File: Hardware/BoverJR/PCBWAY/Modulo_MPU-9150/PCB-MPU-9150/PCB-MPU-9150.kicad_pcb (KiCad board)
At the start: 2 copper layers, 15 x 20 mm, 16 parts, among them P1 CONN_01X08, U1 MPU-9150, U2 AP2112K-3.3

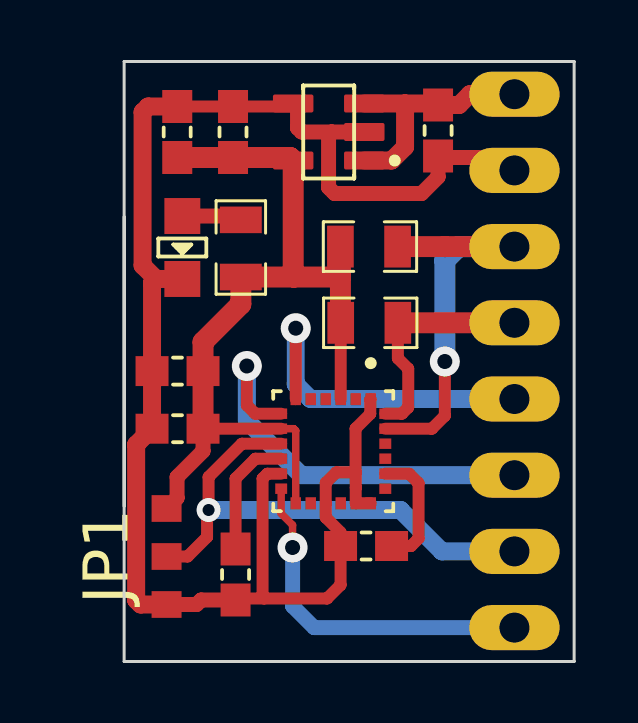
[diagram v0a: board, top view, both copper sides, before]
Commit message: esperando verificacion de pcbway ya cargue 6 gerber
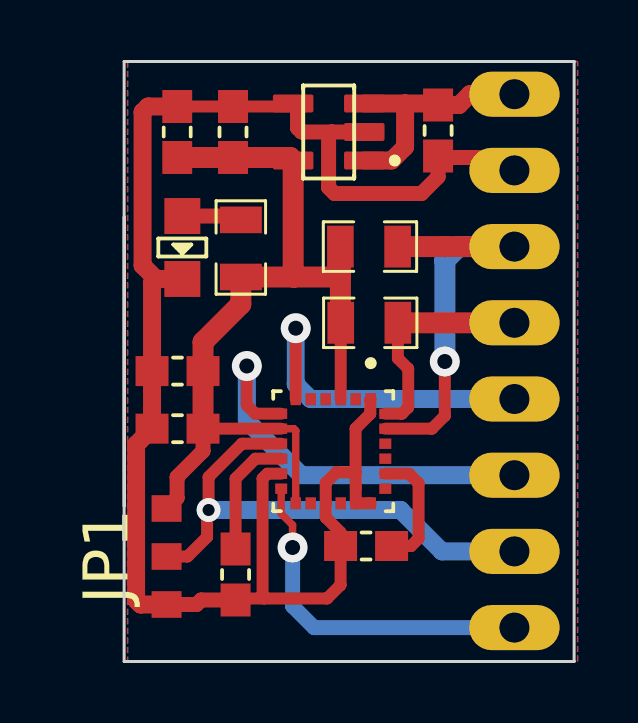
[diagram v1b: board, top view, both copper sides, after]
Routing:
- added copper zone on B.Cu, net GND
- added copper zone on F.Cu, net GND
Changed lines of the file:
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@@
       (psa4output false)
       (plotreference true)
-      (plotvalue true)
+      (plotvalue false)
       (plotinvisibletext false)
       (sketchpadsonfab false)
@@
       (drillshape 0)
       (scaleselection 1)
-      (outputdirectory "Gerber/")
+      (outputdirectory "../../gerber/mpu-modulo/")
     )
   )
@@
     (pts (xy 169.885238 40) (xy 154.885238 40))
     (height 2.5)
-    (gr_text "15,0000 mm" (at 162.385238 36.35) (layer "Dwgs.User")
+    (gr_text "15.0000 mm" (at 162.385238 36.35) (layer "Dwgs.User")
       (effects (font (size 1 1) (thickness 0.15)))
     )
@@
     (pts (xy 154.885238 40) (xy 154.885238 60))
     (height 3.585238)
-    (gr_text "20,0000 mm" (at 150.15 50 90) (layer "Dwgs.User")
+    (gr_text "20.0000 mm" (at 150.15 50 90) (layer "Dwgs.User")
       (effects (font (size 1 1) (thickness 0.15)))
     )
@@
   (segment (start 164.1 54.95) (end 165.48 56.33) (width 0.6) (layer "B.Cu") (net 20))
   (segment (start 165.48 56.33) (end 167.895238 56.33) (width 0.6) (layer "B.Cu") (net 20))
+  (zone (net 1) (net_name "GND") (layers "F&B.Cu") (hatch edge 0.5)
+    (connect_pads (clearance 0.5))
+    (min_thickness 0.25) (filled_areas_thickness no)
+    (fill yes (thermal_gap 0.5) (thermal_bridge_width 0.5))
+    (polygon
+      (pts
+        (xy 170 40)
+        (xy 155 40)
+        (xy 155 60)
+        (xy 170 60)
+      )
+    )
+  )
 )
